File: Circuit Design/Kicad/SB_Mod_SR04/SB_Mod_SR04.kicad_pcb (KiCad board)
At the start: 4 copper layers, 36.1 x 45.1 mm, 25 parts, among them J1 TPs, J2 GND, J3 RESET, U1 ATTINY84A

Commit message: Update before creating dev branch
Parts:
- D3: footprint Diode_SMD:D_SOD-323F -> Diode_SMD:D_SOD-123
- R9: value 1k -> 1K
- moved D3 0.89 mm to (126.5, 95.6)
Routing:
- net +5V: track 13.1 -> 11.7 mm
- net /SB_DAT: track 37.0 -> 36.2 mm
- net /~{SB_INT}: track 29.1 -> 28.5 mm
- net /~{SB_INT}P: track 5.50 -> 4.90 mm
- net /~{SB_ACT}: track 24.9 -> 24.3 mm
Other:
- board text added: "Machina Speculatrix Sensor Bus HC-SR04 Ultrasonic Rangefinder Rev A1 - Sept 2025"
- board text removed: "Machina Speculatrix Sensor Bus HC-SR04 Ultrasonic Rangefinder Rev A1 - Aug 2025"

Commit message: Tidy up
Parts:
- removed D3: SD103C, Diode_SMD:D_SOD-123
- removed SB1: LP_Sensor_Bus_IDC_8, MS_Connectors:SensorBus_2x04_P2.54mm_Vertical
- added CONN2: SENSOR_BUS, MS_Connectors:LP_Sensor_Bus_HE10_2x3, F.Cu at (130.6, 85.9)
- R8: value 22K -> 10K
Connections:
- J1 pad 1: /SB_DAT -> GND
- J1 pad 2: /SB_CLK -> /SB_DAT
- J1 pad 3: /~{SB_ACT} -> /SB_CLK
- J1 pad 4: /~{SB_INT} -> GND
- U1 pad 10: /~{SB_INT}P -> unconnected-(U1-PA3-Pad10)
- U1 pad 11: /~{SB_ACT} -> unconnected-(U1-PA2-Pad11)
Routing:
- net /~{SB_INT}: track 28.5 -> 0.00 mm
- net /~{SB_ACT}: track 24.3 -> 0.00 mm, vias 1 -> 0
- net /~{SB_INT}P: track 4.90 -> 0.00 mm
- net /SB_DAT: track 36.2 -> 37.9 mm, vias 2 -> 1
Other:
- board text added: "GND"
- board text removed: "~{ACT}"
- board text removed: "~{INT}"

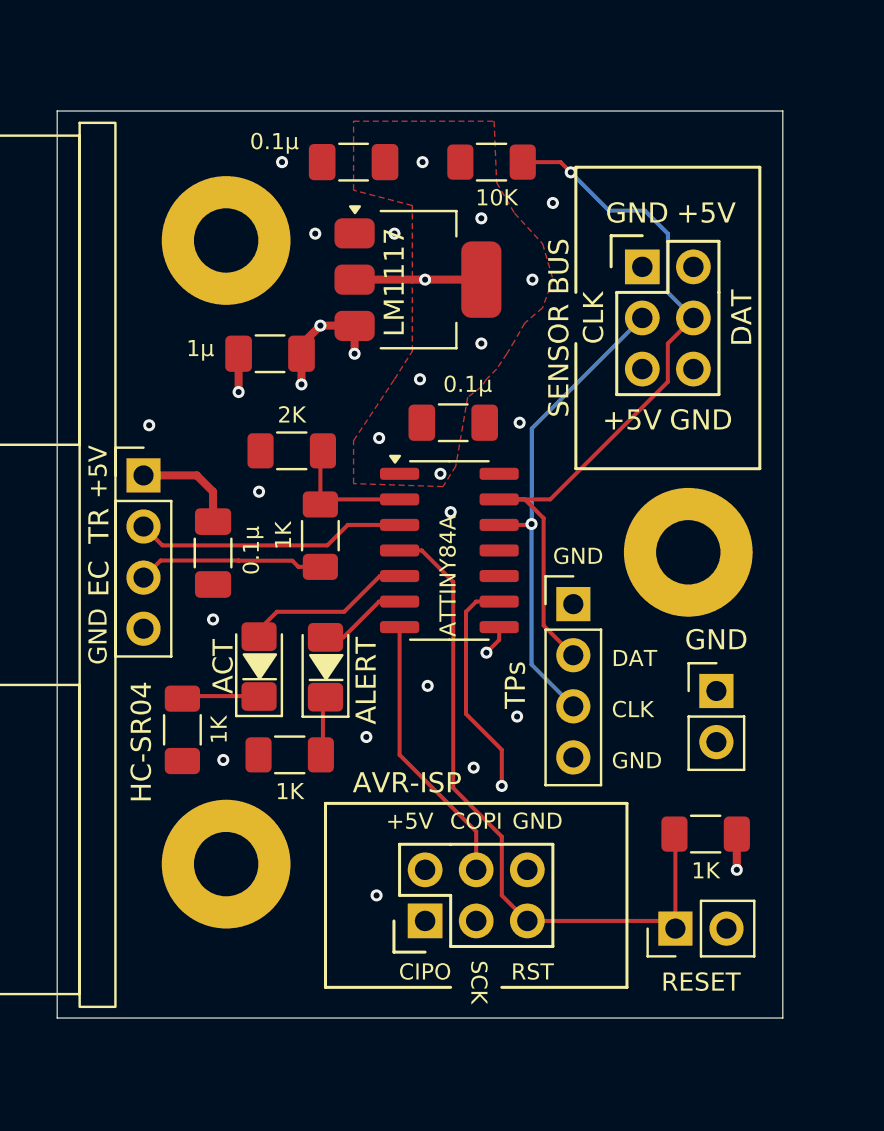
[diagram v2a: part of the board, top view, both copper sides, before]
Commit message: Class-based version of SR04 code. Pausing that here for now.
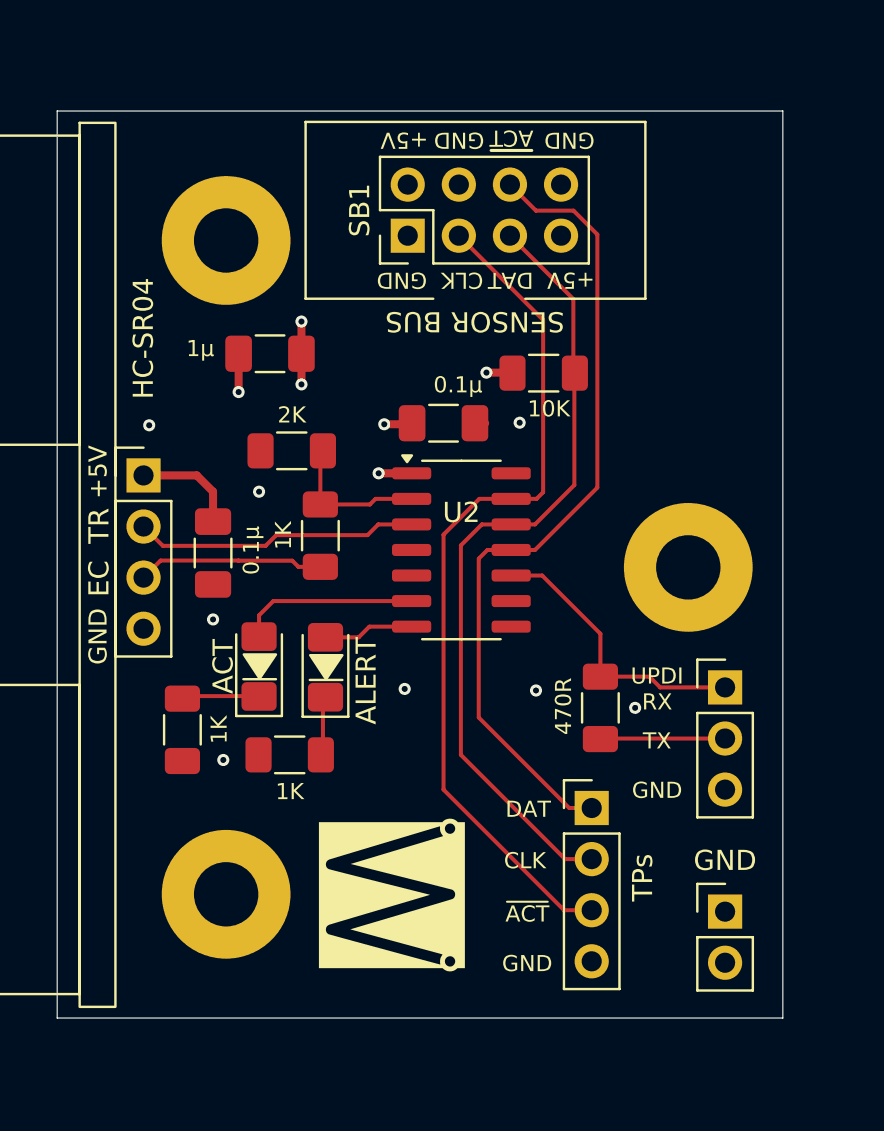
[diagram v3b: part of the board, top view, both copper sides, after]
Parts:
- removed C5: 0.1µ, Capacitor_SMD:C_1206_3216Metric_Pad1.33x1.80mm_HandSolder
- removed CONN1: AVR-ISP, MS_Connectors:AVR_ISP_HE10_2x3
- removed CONN2: SENSOR_BUS, MS_Connectors:LP_Sensor_Bus_HE10_2x3
- removed LM1: LM1117, Package_TO_SOT_SMD:SOT-223-3_TabPin2
- removed U1: ATTINY84A, Package_SO:SOIC-14_3.9x8.7mm_P1.27mm
- added G***: LOGO, MS_General:MS-logo, F.Cu at (116.8, 114.6)
- added SB1: LP_Sensor_Bus_IDC_8, MS_Connectors:SensorBus_2x04_P2.54mm_Vertical, F.Cu at (115.8, 77.5)
- added U2: ATtiny1604, Package_SO:SOIC-14_3.9x8.7mm_P1.27mm, F.Cu at (120.3, 97.4)
- J1: value TPs -> UPDI; footprint Connector_PinHeader_2.54mm:PinHeader_1x04_P2.54mm_Vertical -> Connector_PinHeader_2.54mm:PinHeader_1x03_P2.54mm_Vertical
- J3: value RESET -> TPs; footprint Connector_PinHeader_2.54mm:PinHeader_1x02_P2.54mm_Vertical -> Connector_PinHeader_2.54mm:PinHeader_1x04_P2.54mm_Vertical
- R2: value 1K -> 470R
- moved J2 11.0 mm to (133.4, 115.4)
- moved R8 10.8 mm to (124.4, 88.6)
- moved J1 8.61 mm to (133.4, 104.2)
- moved R2 8.17 mm to (127.2, 105.2), turned to 90 degrees
- moved J3 7.30 mm to (126.8, 110.2), turned to 0 degrees
- moved H3 1.50 mm to (108.6, 114.5)
- moved H2 0.75 mm to (131.6, 98.2)
- moved C4 0.48 mm to (119.4, 91.1)
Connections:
- C4 pad 1: +3V3 -> +5V
- J1 pad 1: GND -> /UPDI
- J1 pad 2: /SB_DAT -> /PROG_TX
- J1 pad 3: /SB_CLK -> GND
- J3 pad 1: /~{RESET} -> /SB_ACT
- J3 pad 2: GND -> /SB_DAT
- R2 pad 1: /~{RESET} -> /PROG_TX
- R2 pad 2: +3V3 -> /UPDI
- R8 pad 2: +3V3 -> +5V
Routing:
- net /SB_ACT: track 0.00 -> 40.7 mm
- net /~{RESET}: track 33.9 -> 0.00 mm
- net /SB_CLK: track 24.0 -> 42.8 mm, vias 1 -> 0
- net /SCK: track 18.4 -> 0.00 mm, vias 1 -> 0
- net /CIPO: track 16.1 -> 0.00 mm, vias 1 -> 0
- net /UPDI: track 0.00 -> 14.2 mm
- net /COPI: track 13.6 -> 0.00 mm
- net +3V3: track 8.08 -> 0.00 mm, vias 9 -> 0
- net /PROG_TX: track 0.00 -> 6.21 mm
- net /SB_DAT: track 37.9 -> 39.7 mm, vias 1 -> 0
- net +5V: track 11.7 -> 12.8 mm, vias 3 -> 5
- net /ACT_LED: track 8.09 -> 8.93 mm
- net /ECHO_L: track 6.76 -> 7.37 mm
- net GND: track 2.43 -> 2.45 mm, vias 16 -> 9
- added copper zone on B.Cu, net +5V
- removed copper zone on B.Cu, net +3V3
- removed copper zone on F.Cu, net +3V3
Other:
- board text added: "TX"
- board text added: "UPDI RX"
- board text added: "~{ACT}"

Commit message: Reorganised
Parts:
- removed the G*** at (116.8, 114.6)
- removed the G*** at (115.8, 97.7)
- removed R10: 2K, MS_Favourites:Resistor_SMD_1206_HandSolder
- removed R9: 1K, MS_Favourites:Resistor_SMD_1206_HandSolder
- added CONN1: AVR-UPDI-ICE, Connector_PinHeader_2.54mm:PinHeader_2x03_P2.54mm_Vertical, F.Cu at (126.4, 110.3)
- added D3: SD103C, Diode_SMD:D_SOD-123, F.Cu at (127.3, 105.2)
- added G***: LOGO, MS_General:MS-logo, F.Cu at (131.7, 89.8)
- added J4: SERIAL, Connector_PinHeader_2.54mm:PinHeader_1x03_P2.54mm_Vertical, F.Cu at (114.4, 116.7)
- added J5: GPIO, Connector_PinHeader_2.54mm:PinHeader_1x02_P2.54mm_Vertical, F.Cu at (113.3, 89.4)
- R2: value 470R -> 10K
- moved C2 20.5 mm to (130.9, 83.3), turned to -90 degrees
- moved J2 11.3 mm to (122.3, 117.2), turned to -90 degrees
- moved J3 7.88 mm to (120.9, 104.9)
- moved R2 7.13 mm to (126.5, 98.1)
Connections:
- A1 pad 3: /ECHO_H -> /ECHO
- R2 pad 1: /PROG_TX -> /UPDI
- R2 pad 2: /UPDI -> +5V
- U2 pad 2: /ECHO_L -> /TRIG
- U2 pad 3: /TRIG -> /ECHO
- U2 pad 4: unconnected-(U2-PA6-Pad4) -> /A6
- U2 pad 5: unconnected-(U2-PA7-Pad5) -> /A7
- U2 pad 6: /ACT_LED -> /RX
- U2 pad 7: /ALERT_LED -> /TX
- U2 pad 8: unconnected-(U2-PB1-Pad8) -> /ACT_LED
- U2 pad 9: unconnected-(U2-PB0-Pad9) -> /ALERT_LED
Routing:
- net /TX: track 0.00 -> 17.3 mm
- net /RX: track 0.00 -> 16.6 mm
- net /ECHO: track 0.00 -> 14.4 mm
- net /A7: track 0.00 -> 13.9 mm, vias 0 -> 1
- net /A6: track 0.00 -> 11.2 mm, vias 0 -> 1
- net /ALERT_LED: track 4.50 -> 13.9 mm, vias 0 -> 2
- net /ECHO_H: track 9.27 -> 0.00 mm
- net /UPDI: track 14.2 -> 22.3 mm
- net /SB_CLK: track 42.8 -> 34.9 mm
- net /SB_DAT: track 39.7 -> 31.7 mm
- net /SB_ACT: track 40.7 -> 33.2 mm
- net /ECHO_L: track 7.37 -> 0.00 mm
- net /ACT_LED: track 8.93 -> 14.9 mm, vias 0 -> 2
- net +5V: track 12.8 -> 15.4 mm, vias 5 -> 6
- net GND: track 2.45 -> 0.55 mm, vias 9 -> 15
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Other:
- board size 36.1 x 45.1 mm -> 36.1 x 45 mm
- board text added: "A6"
- board text added: "A7"
- board text added: "Machina Speculatrix Sensor Bus HC-SR04 Ultrasonic Rangefinder Rev A1 - Dec 2025"
- board text added: "RX"
- board text added: "SERIAL"
- board text added: "UPDI"
- board text removed: "Machina Speculatrix Sensor Bus HC-SR04 Ultrasonic Rangefinder Rev A1 - Sept 2025"
